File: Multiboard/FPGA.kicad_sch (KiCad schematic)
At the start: 68 parts, among them J6 Conn_02x20_Odd_Even, J7 Conn_02x20_Odd_Even, J8 USB_C_Receptacle_USB2.0_16P, U6 LCMXO2-1200ZE-1TG144C, U7 FAN1112, U8 NCP1117

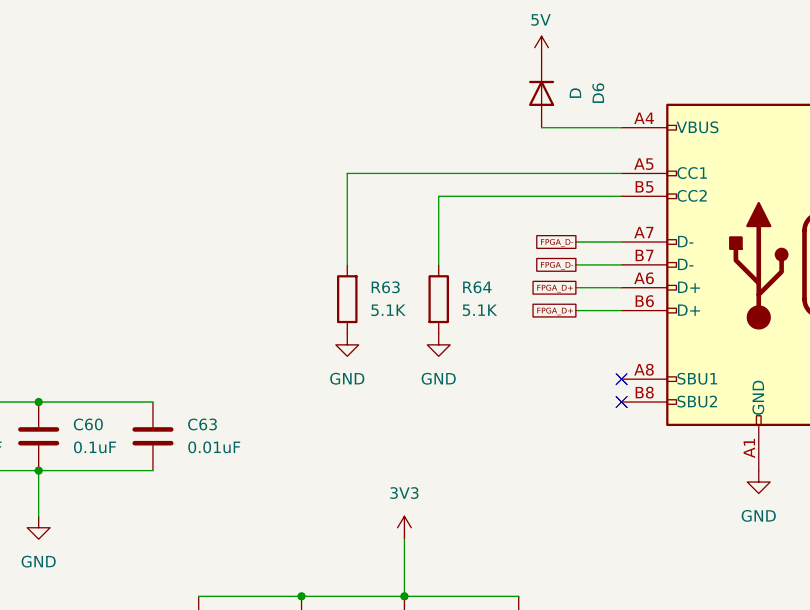
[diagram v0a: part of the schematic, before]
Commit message: Completed mcu usb-c, mcu oscillators and mcu jtag pins
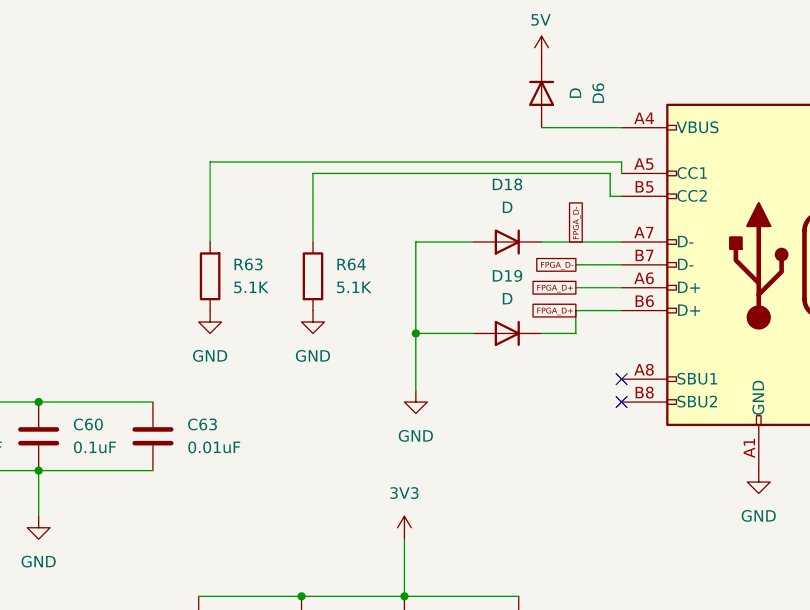
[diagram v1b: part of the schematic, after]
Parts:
- added D18, D19: D, Diode_SMD:D_0603_1608Metric_Pad1.05x0.95mm_HandSolder, symbol Device:D
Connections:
- net FPGA_D+: now also D19.1 (K)
- net FPGA_D-: now also D18.1 (K)
- net GND: now also D18.2 (A), D19.2 (A)
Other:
- moved on the sheet: R63, R64

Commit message: positioned and wired FTDI
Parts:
- J6, J7: footprint Connector_IDC:IDC-Header_2x20_P2.54mm_Vertical -> Connector_IDC:IDC-Header_2x20_P2.54mm_Latch_Vertical
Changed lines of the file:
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@@
 			)
 		)
-		(property "Footprint" "Connector_IDC:IDC-Header_2x20_P2.54mm_Vertical"
+		(property "Footprint" "Connector_IDC:IDC-Header_2x20_P2.54mm_Latch_Vertical"
 			(at 269.24 64.77 0)
 			(effects
@@
 			)
 		)
-		(property "Footprint" "Connector_IDC:IDC-Header_2x20_P2.54mm_Vertical"
+		(property "Footprint" "Connector_IDC:IDC-Header_2x20_P2.54mm_Latch_Vertical"
 			(at 87.63 62.23 0)
 			(effects

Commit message: synchronised sch and pcb. Added jtag connection between fpga and ftdi
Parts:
- removed C44, C45, C46, C47, C58, C59, C60, C66: 0.1uF, Capacitor_SMD:C_0603_1608Metric_Pad1.08x0.95mm_HandSolder, symbol Device:C
- removed C64: 10uF, Capacitor_SMD:C_0603_1608Metric_Pad1.08x0.95mm_HandSolder, symbol Device:C
- removed C65: 1uF, Capacitor_SMD:C_0603_1608Metric_Pad1.08x0.95mm_HandSolder, symbol Device:C
- removed C67: 0.01uF, Capacitor_SMD:C_0603_1608Metric_Pad1.08x0.95mm_HandSolder, symbol Device:C
- renumbered C48 to C44, C49 to C45, C50 to C46, C51 to C47, C52 to C48, C53 to C49, C54 to C50, C55 to C51, C56 to C52, C57 to C53, C61 to C54, C62 to C55, C63 to C56, R61 to R57, R62 to R58, R63 to R59, R64 to R60, R65 to R61, R66 to R62, R67 to R63, R68 to R64, R69 to R65, R70 to R66, R71 to R67, R72 to R68, R73 to R69, R74 to R70, R75 to R71, R76 to R72
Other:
- moved on the sheet: C37, C41, C47, C53, C54, C55, C56

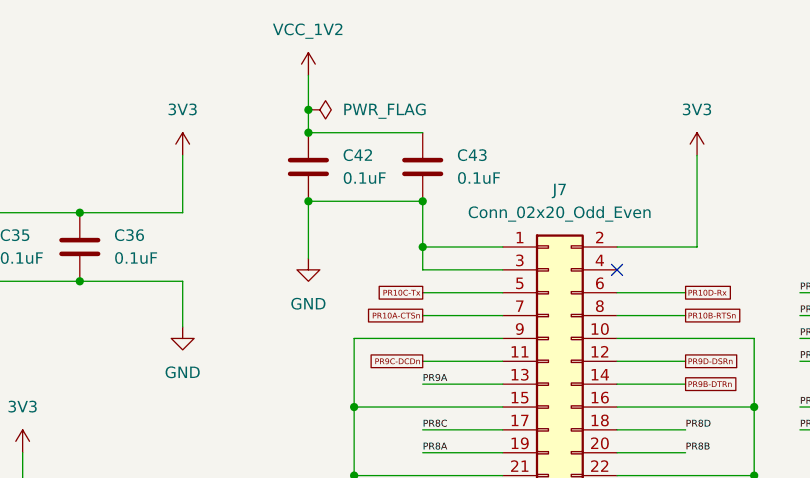
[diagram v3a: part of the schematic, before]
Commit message: positioned ldo's and wired a few pins
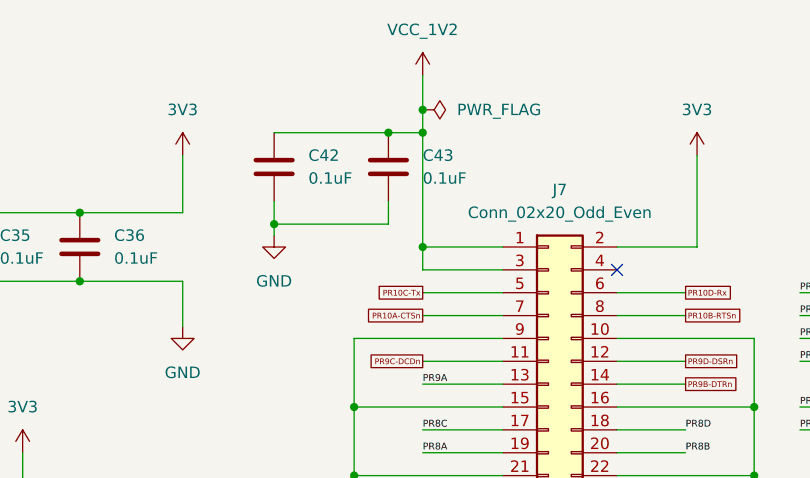
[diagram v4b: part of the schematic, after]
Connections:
- net GND: no longer J7.1 (Pin_1), J7.3 (Pin_3)
- net VCC_1V2: now also J7.1 (Pin_1), J7.3 (Pin_3)
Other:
- moved on the sheet: C42, C43

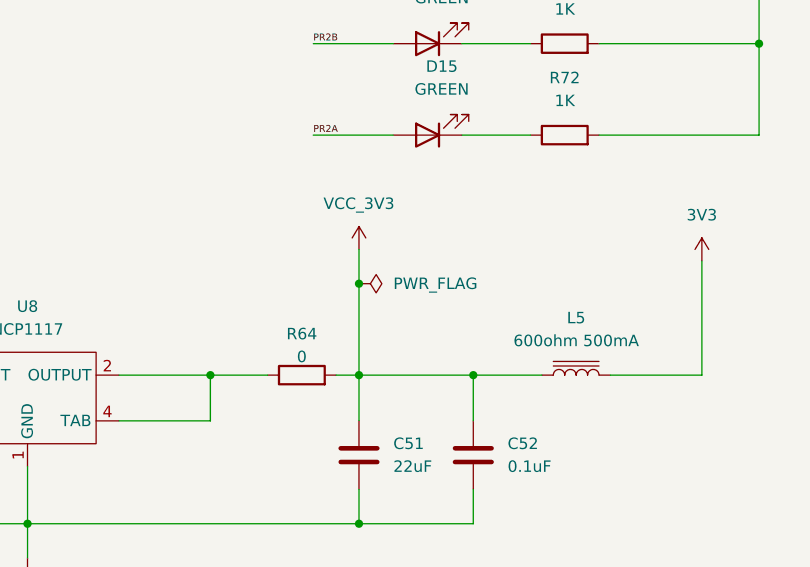
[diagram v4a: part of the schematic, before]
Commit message: wired power traces and added prototype area
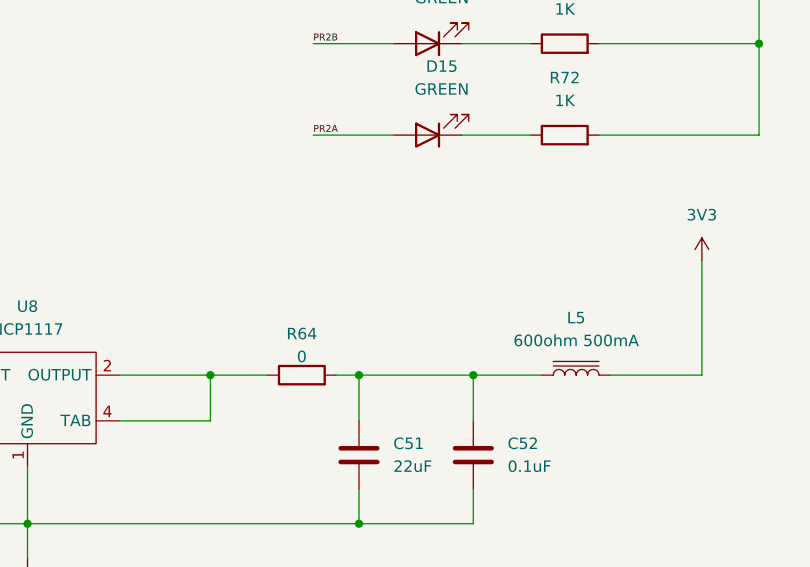
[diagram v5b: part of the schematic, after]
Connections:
- net VCC_3V3: no longer names the net of C51.1, C52.1, L5.1, R64.2
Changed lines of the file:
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@@
 	)
 	(junction
-		(at 114.3 196.85)
-		(diameter 0)
-		(color 0 0 0 0)
-	)
-	(junction
 		(at 158.75 139.7)
 		(diameter 0)
@@
 	(wire
 		(pts
-			(xy 114.3 196.85) (xy 114.3 207.01)
-		)
-		(stroke
-			(width 0)
-			(type default)
-		)
-	)
-	(wire
-		(pts
 			(xy 345.44 49.53) (xy 350.52 49.53)
 		)
@@
 	(wire
 		(pts
-			(xy 114.3 193.04) (xy 114.3 196.85)
-		)
-		(stroke
-			(width 0)
-			(type default)
-		)
-	)
-	(wire
-		(pts
 			(xy 196.85 73.66) (xy 196.85 69.85)
 		)
@@
 	)
 	(symbol
-		(lib_id "power:VCC")
-		(at 114.3 193.04 0)
-		(unit 1)
-		(exclude_from_sim no)
-		(in_bom yes)
-		(on_board yes)
-		(dnp no)
-		(fields_autoplaced yes)
-		(property "Reference" "#PWR083"
-			(at 114.3 196.85 0)
-			(effects
-				(font
-					(size 1.27 1.27)
-				)
-				(hide yes)
-			)
-		)
-		(property "Value" "VCC_3V3"
-			(at 114.3 187.96 0)
-			(effects
-				(font
-					(size 1.27 1.27)
-				)
-			)
-		)
-		(property "Footprint" ""
-			(at 114.3 193.04 0)
-			(effects
-				(font
-					(size 1.27 1.27)
-				)
-				(hide yes)
-			)
-		)
-		(property "Datasheet" ""
-			(at 114.3 193.04 0)
-			(effects
-				(font
-					(size 1.27 1.27)
-				)
-				(hide yes)
-			)
-		)
-		(property "Description" "Power symbol creates a global label with name \"VCC\""
-			(at 114.3 193.04 0)
-			(effects
-				(font
-					(size 1.27 1.27)
-				)
-				(hide yes)
-			)
-		)
-		(pin "1"
-		)
-		(instances
-			(project ""
-				(path "/9ed4a389-3aa7-41f1-b239-280eb7f09ef1/a1879700-d4ae-4f4f-b9ed-53e5618d969d"
-					(reference "#PWR083")
-					(unit 1)
-				)
-			)
-		)
-	)
-	(symbol
 		(lib_id "Device:R")
 		(at 137.16 180.34 90)
@@
 					(unit 1)
 				)
-			)
-		)
-	)
-	(symbol
-		(lib_id "power:PWR_FLAG")
-		(at 114.3 196.85 270)
-		(unit 1)
-		(exclude_from_sim no)
-		(in_bom yes)
-		(on_board yes)
-		(dnp no)
-		(fields_autoplaced yes)
-		(property "Reference" "#FLG08"
-			(at 116.205 196.85 0)
-			(effects
-				(font
-					(size 1.27 1.27)
-				)
-				(hide yes)
-			)
-		)
-		(property "Value" "PWR_FLAG"
-			(at 118.11 196.8499 90)
-			(effects
-				(font
-					(size 1.27 1.27)
-				)
-				(justify left)
-			)
-		)
-		(property "Footprint" ""
-			(at 114.3 196.85 0)
-			(effects
-				(font
-					(size 1.27 1.27)
-				)
-				(hide yes)
-			)
-		)
-		(property "Datasheet" "~"
-			(at 114.3 196.85 0)
-			(effects
-				(font
-					(size 1.27 1.27)
-				)
-				(hide yes)
-			)
-		)
-		(property "Description" "Special symbol for telling ERC where power comes from"
-			(at 114.3 196.85 0)
-			(effects
-				(font
-					(size 1.27 1.27)
-				)
-				(hide yes)
-			)
-		)
-		(pin "1"
-		)
-		(instances
-			(project ""
-				(path "/9ed4a389-3aa7-41f1-b239-280eb7f09ef1/a1879700-d4ae-4f4f-b9ed-53e5618d969d"
-					(reference "#FLG08")
-					(unit 1)
-				)

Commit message: fixed fpga header issue
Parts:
- J7: footprint Connector_IDC:IDC-Header_2x20_P2.54mm_Latch_Vertical -> Connector_PinHeader_2.00mm:PinHeader_2x20_P2.00mm_Vertical
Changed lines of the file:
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@@
 			)
 		)
-		(property "Footprint" "Connector_IDC:IDC-Header_2x20_P2.54mm_Latch_Vertical"
+		(property "Footprint" "Connector_PinHeader_2.00mm:PinHeader_2x20_P2.00mm_Vertical"
 			(at 269.24 64.77 0)
 			(effects

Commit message: fixed switch and led issue
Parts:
- J6: footprint Connector_IDC:IDC-Header_2x20_P2.54mm_Latch_Vertical -> Connector_PinHeader_2.54mm:PinHeader_2x20_P2.54mm_Vertical
- J7: footprint Connector_PinHeader_2.00mm:PinHeader_2x20_P2.00mm_Vertical -> Connector_PinHeader_2.54mm:PinHeader_2x20_P2.54mm_Vertical
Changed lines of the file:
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@@
 			)
 		)
-		(property "Footprint" "Connector_PinHeader_2.00mm:PinHeader_2x20_P2.00mm_Vertical"
+		(property "Footprint" "Connector_PinHeader_2.54mm:PinHeader_2x20_P2.54mm_Vertical"
 			(at 269.24 64.77 0)
 			(effects
@@
 			)
 		)
-		(property "Footprint" "Connector_IDC:IDC-Header_2x20_P2.54mm_Latch_Vertical"
+		(property "Footprint" "Connector_PinHeader_2.54mm:PinHeader_2x20_P2.54mm_Vertical"
 			(at 87.63 62.23 0)
 			(effects

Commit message: cleared part of errors and warnings
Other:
- company: (none) -> Technological School "Electronic Systems"
- title: (none) -> IR-Multiboard/FPGA
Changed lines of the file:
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@@
 	(generator_version "9.0")
 	(paper "A3")
+	(title_block
+		(title "IR-Multiboard/FPGA")
+		(date "2026-02-23")
+		(company "Technological School \"Electronic Systems\"")
+	)
 	(junction
 		(at 127 247.65)
